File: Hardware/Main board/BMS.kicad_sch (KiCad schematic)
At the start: 14 parts, among them U1 BQ25895RTW

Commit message: Big changes
- Folder changes
- change dimensions of board to match thicker material
- begin part selection/footprint selection
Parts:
- C1, C3: footprint (none) -> Capacitor_SMD:C_0402_1005Metric
- C2, C5, C6: footprint (none) -> Capacitor_SMD:C_0603_1608Metric
- C4: footprint (none) -> Capacitor_SMD:C_1206_3216Metric
- D1: footprint (none) -> Diode_SMD:D_0603_1608Metric
- L1: footprint (none) -> Inductor_SMD:L_1210_3225Metric
- R1, R2: footprint (none) -> Resistor_SMD:R_0603_1608Metric
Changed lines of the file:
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@@
 			)
 		)
-		(property "Footprint" ""
+		(property "Footprint" "Capacitor_SMD:C_0603_1608Metric"
 			(at 214.63 64.77 0)
 			(effects
@@
 			)
 		)
-		(property "Footprint" ""
+		(property "Footprint" "Capacitor_SMD:C_0603_1608Metric"
 			(at 177.8 76.2 0)
 			(effects
@@
 			)
 		)
-		(property "Footprint" ""
+		(property "Footprint" "Resistor_SMD:R_0603_1608Metric"
 			(at 180.34 87.63 0)
 			(effects
@@
 			)
 		)
-		(property "Footprint" ""
+		(property "Footprint" "Capacitor_SMD:C_0603_1608Metric"
 			(at 201.93 64.77 0)
 			(effects
@@
 			)
 		)
-		(property "Footprint" ""
+		(property "Footprint" "Capacitor_SMD:C_1206_3216Metric"
 			(at 187.96 46.99 0)
 			(effects
@@
 			)
 		)
-		(property "Footprint" ""
+		(property "Footprint" "Diode_SMD:D_0603_1608Metric"
 			(at 181.61 57.15 90)
 			(effects
@@
 			)
 		)
-		(property "Footprint" ""
+		(property "Footprint" "Capacitor_SMD:C_0402_1005Metric"
 			(at 146.05 46.99 0)
 			(effects
@@
 			)
 		)
-		(property "Footprint" ""
+		(property "Footprint" "Inductor_SMD:L_1210_3225Metric"
 			(at 190.5 59.69 0)
 			(effects
@@
 			)
 		)
-		(property "Footprint" ""
+		(property "Footprint" "Capacitor_SMD:C_0402_1005Metric"
 			(at 181.61 63.5 0)
 			(effects
@@
 			)
 		)
-		(property "Footprint" ""
+		(property "Footprint" "Resistor_SMD:R_0603_1608Metric"
 			(at 180.34 92.71 0)
 			(effects

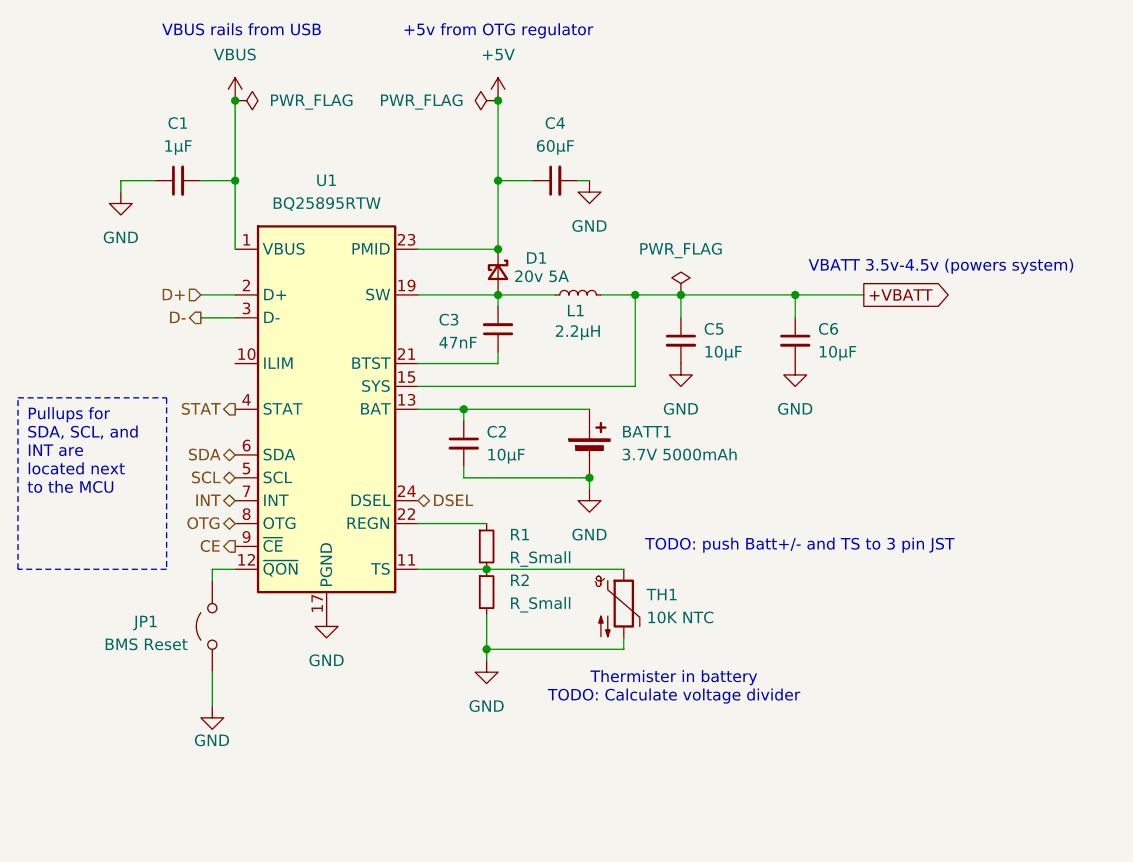
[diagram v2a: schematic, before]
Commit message: hardware changes and initial traces/layout
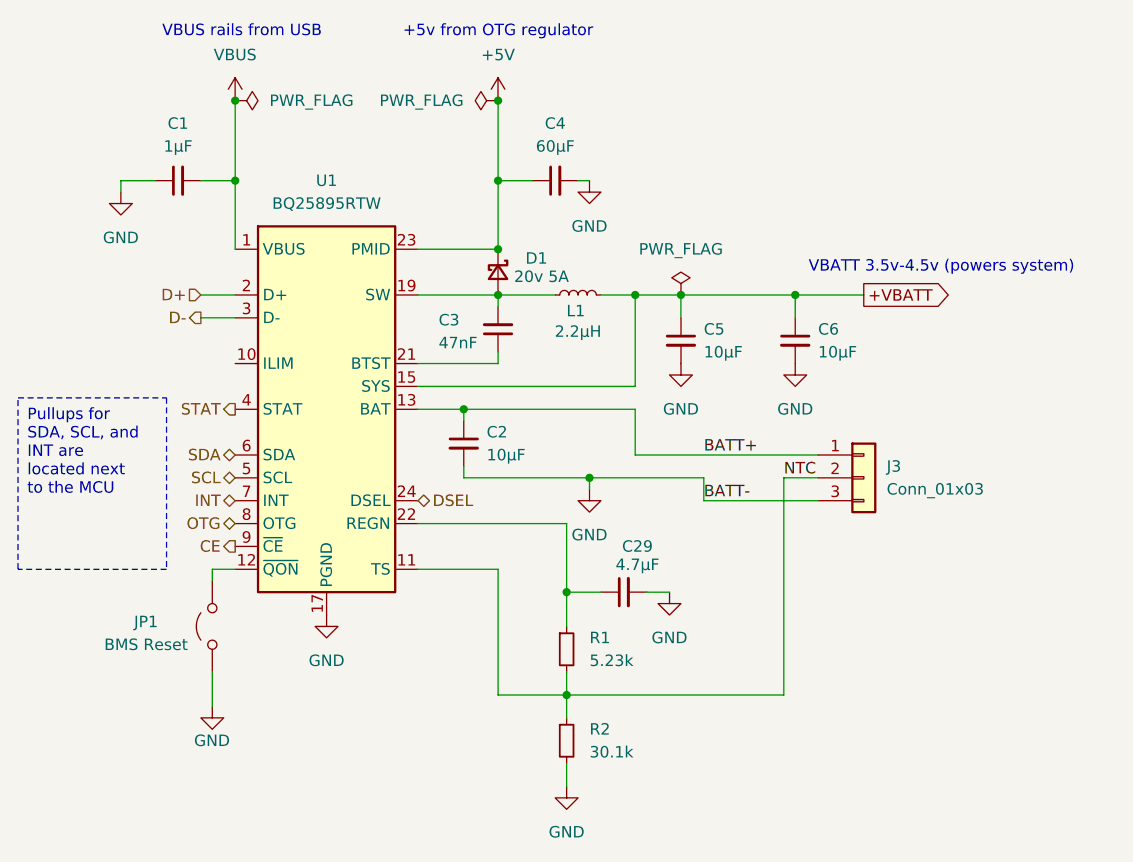
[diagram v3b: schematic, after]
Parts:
- removed BATT1: 3.7V 5000mAh, symbol Device:Battery_Cell
- removed TH1: 10K NTC, symbol Device:Thermistor_NTC
- added C29: 4.7μF, symbol Device:C_Small
- added J3: Conn_01x03, symbol Connector_Generic:Conn_01x03
- R1: value R_Small -> 5.23k
- R2: value R_Small -> 30.1k
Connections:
- net GND: now also C29.2, J3.3 (Pin_3)
- net BATT+: now reaches C2.1, U1.13 (BAT), U1.14 (BAT)
- net BATT+: now also J3.1 (Pin_1)
- net at R1.1, U1.22 (REGN): now also C29.1
- net NTC: now reaches R1.2, R2.1, U1.11 (TS)
- net NTC: now also J3.2 (Pin_2)
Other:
- note removed: "TODO: push Batt+/- and TS to 3 pin JST"
- note removed: "Thermister in battery TODO: Calculate voltage divider"
- moved on the sheet: R1, R2

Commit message: Add Crystal
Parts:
- C29: footprint (none) -> Capacitor_SMD:C_0603_1608Metric
- J3: footprint (none) -> Connector_JST:JST_XH_S3B-XH-SM4-TB_1x03-1MP_P2.50mm_Horizontal
- JP1: footprint (none) -> TestPoint:TestPoint_2Pads_Pitch5.08mm_Drill1.3mm
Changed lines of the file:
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@@
 			)
 		)
-		(property "Footprint" ""
+		(property "Footprint" "TestPoint:TestPoint_2Pads_Pitch5.08mm_Drill1.3mm"
 			(at 149.86 96.52 0)
 			(effects
@@
 			)
 		)
-		(property "Footprint" ""
+		(property "Footprint" "Capacitor_SMD:C_0603_1608Metric"
 			(at 195.58 92.71 0)
 			(effects
@@
 			)
 		)
-		(property "Footprint" ""
+		(property "Footprint" "Connector_JST:JST_XH_S3B-XH-SM4-TB_1x03-1MP_P2.50mm_Horizontal"
 			(at 222.25 80.01 0)
 			(effects

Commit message: Finish routing
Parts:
- JP1: value BMS Reset -> BMS_RESET; footprint TestPoint:TestPoint_2Pads_Pitch5.08mm_Drill1.3mm -> Jumper:SolderJumper-2_P1.3mm_Open_RoundedPad1.0x1.5mm
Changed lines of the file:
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@@
 			)
 		)
-		(property "Value" "BMS Reset"
+		(property "Value" "BMS_RESET"
 			(at 142.494 98.552 90)
 			(effects
@@
 			)
 		)
-		(property "Footprint" "TestPoint:TestPoint_2Pads_Pitch5.08mm_Drill1.3mm"
+		(property "Footprint" "Jumper:SolderJumper-2_P1.3mm_Open_RoundedPad1.0x1.5mm"
 			(at 149.86 96.52 0)
 			(effects

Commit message: Add resistor for ILIM pin
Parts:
- added R8: 260, Resistor_SMD:R_0402_1005Metric, symbol Device:R_Small
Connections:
- net GND: now also R8.1
- net at U1.10 (ILIM): now also R8.2
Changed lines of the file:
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@@
 	(wire
 		(pts
+			(xy 140.97 67.31) (xy 152.4 67.31)
+		)
+		(stroke
+			(width 0)
+			(type default)
+		)
+	)
+	(wire
+		(pts
 			(xy 189.23 92.71) (xy 189.23 85.09)
 		)
@@
 	(wire
 		(pts
+			(xy 135.89 69.85) (xy 135.89 67.31)
+		)
+		(stroke
+			(width 0)
+			(type default)
+		)
+	)
+	(wire
+		(pts
 			(xy 193.04 59.69) (xy 196.85 59.69)
 		)
@@
 	(text_box "Pullups for SDA, SCL, and INT are located next to the MCU"
 		(exclude_from_sim no)
-		(at 128.27 71.12 0)
-		(size 16.51 19.05)
+		(at 130.81 80.01 0)
+		(size 16.51 12.7)
 		(stroke
 			(width 0)
@@
 	(symbol
 		(lib_id "power:GND")
+		(at 135.89 69.85 0)
+		(unit 1)
+		(exclude_from_sim no)
+		(in_bom yes)
+		(on_board yes)
+		(dnp no)
+		(fields_autoplaced yes)
+		(property "Reference" "#PWR046"
+			(at 135.89 76.2 0)
+			(effects
+				(font
+					(size 1.27 1.27)
+				)
+				(hide yes)
+			)
+		)
+		(property "Value" "GND"
+			(at 135.89 74.93 0)
+			(effects
+				(font
+					(size 1.27 1.27)
+				)
+			)
+		)
+		(property "Footprint" ""
+			(at 135.89 69.85 0)
+			(effects
+				(font
+					(size 1.27 1.27)
+				)
+				(hide yes)
+			)
+		)
+		(property "Datasheet" ""
+			(at 135.89 69.85 0)
+			(effects
+				(font
+					(size 1.27 1.27)
+				)
+				(hide yes)
+			)
+		)
+		(property "Description" "Power symbol creates a global label with name \"GND\" , ground"
+			(at 135.89 69.85 0)
+			(effects
+				(font
+					(size 1.27 1.27)
+				)
+				(hide yes)
+			)
+		)
+		(pin "1"
+		)
+		(instances
+			(project ""
+				(path "/e5119d15-74fb-4259-abbc-5cab1f368532/ffb3e92b-c9a0-4fa4-9e23-60cee07ab96a"
+					(reference "#PWR046")
+					(unit 1)
+				)
+			)
+		)
+	)
+	(symbol
+		(lib_id "power:GND")
 		(at 191.77 81.28 0)
 		(unit 1)
@@
 					(unit 1)
 				)
+			)
+		)
+	)
+	(symbol
+		(lib_id "Device:R_Small")
+		(at 138.43 67.31 90)
+		(unit 1)
+		(exclude_from_sim no)
+		(in_bom yes)
+		(on_board yes)
+		(dnp no)
+		(fields_autoplaced yes)
+		(property "Reference" "R8"
+			(at 138.43 62.23 90)
+			(effects
+				(font
+					(size 1.27 1.27)
+				)
+			)
+		)
+		(property "Value" "260"
+			(at 138.43 64.77 90)
+			(effects
+				(font
+					(size 1.27 1.27)
+				)
+			)
+		)
+		(property "Footprint" "Resistor_SMD:R_0402_1005Metric"
+			(at 138.43 67.31 0)
+			(effects
+				(font
+					(size 1.27 1.27)
+				)
+				(hide yes)
+			)
+		)
+		(property "Datasheet" "~"
+			(at 138.43 67.31 0)
+			(effects
+				(font
+					(size 1.27 1.27)
+				)
+				(hide yes)
+			)
+		)
+		(property "Description" "Resistor, small symbol"
+			(at 138.43 67.31 0)
+			(effects
+				(font
+					(size 1.27 1.27)
+				)
+				(hide yes)
+			)
+		)
+		(pin "2"
+		)
+		(pin "1"
+		)
+		(instances
+			(project ""
+				(path "/e5119d15-74fb-4259-abbc-5cab1f368532/ffb3e92b-c9a0-4fa4-9e23-60cee07ab96a"
+					(reference "R8")
+					(unit 1)
+				)

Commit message: Part selection
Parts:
- J3: JLCPCB Part # (none) -> C161860; LCSC Part # (none) -> C161860
- R8: value 260 -> 260Ω
- U1: JLCPCB Part # (none) -> C80200; LCSC Part # (none) -> C80200
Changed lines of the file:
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@@
+			)
+		)
+		(property "JLCPCB Part #" "C80200 "
+			(at 162.56 72.39 0)
+			(effects
+				(font
+					(size 1.27 1.27)
+				)
+				(hide yes)
+			)
+		)
+		(property "LCSC Part #" "C80200 "
+			(at 162.56 72.39 0)
+			(effects
+				(font
+					(size 1.27 1.27)
+				)
+				(hide yes)
 			)
 		)
@@
 			)
 		)
+		(property "JLCPCB Part #" "C161860"
+			(at 222.25 80.01 0)
+			(effects
+				(font
+					(size 1.27 1.27)
+				)
+				(hide yes)
+			)
+		)
+		(property "LCSC Part #" "C161860"
+			(at 222.25 80.01 0)
+			(effects
+				(font
+					(size 1.27 1.27)
+				)
+				(hide yes)
+			)
+		)
 		(pin "2"
 		)
@@
 			)
 		)
-		(property "Value" "260"
+		(property "Value" "260Ω"
 			(at 138.43 64.77 90)
 			(effects

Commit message: Swap 260Ω footprint for 0805
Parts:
- R8: footprint Resistor_SMD:R_0402_1005Metric -> Resistor_SMD:R_0805_2012Metric
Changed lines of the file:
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@@
 			)
 		)
-		(property "Footprint" "Resistor_SMD:R_0402_1005Metric"
+		(property "Footprint" "Resistor_SMD:R_0805_2012Metric"
 			(at 138.43 67.31 0)
 			(effects
